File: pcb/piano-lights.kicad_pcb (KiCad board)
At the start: 2 copper layers, 98 x 51.6 mm, 41 parts, among them J1 USB-C 6-Pin, J2 FTDI RS232, J3 LED Strip, J4 AVR-ISP-6, J5 MIDI IN, J6 MIDI THRU, J7 MIDI Coupler B, J8 MIDI Coupler A, SW1 Button, SW2 Reset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

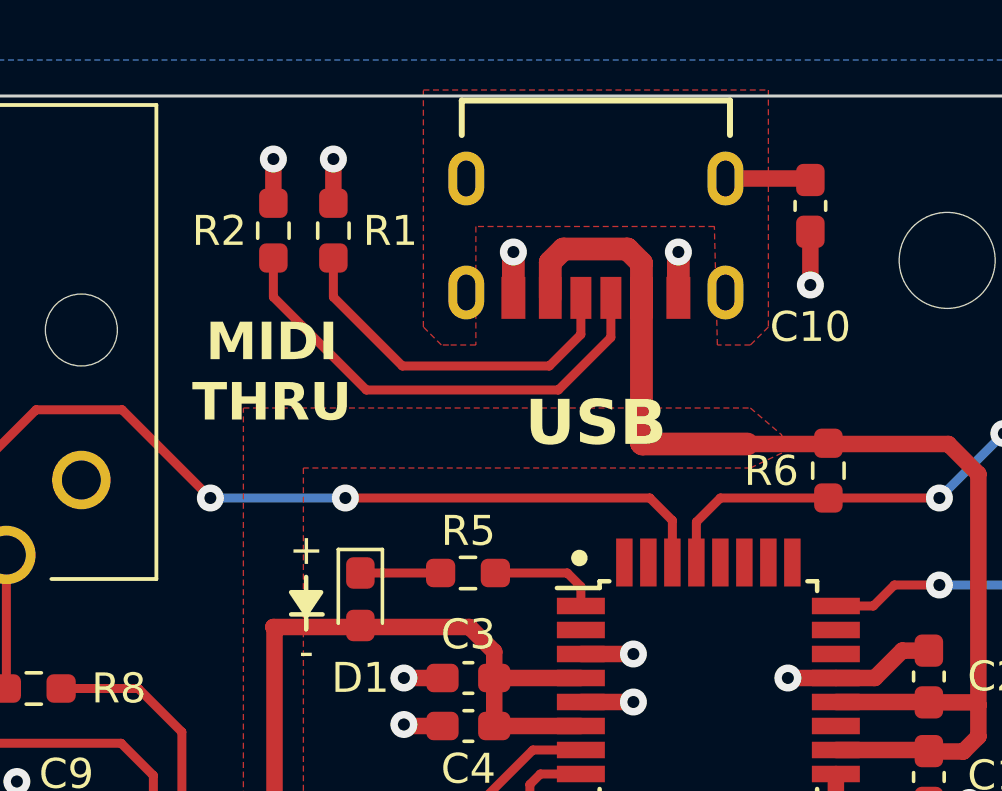
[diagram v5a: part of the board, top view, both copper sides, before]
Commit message: Move R1 and R2 again
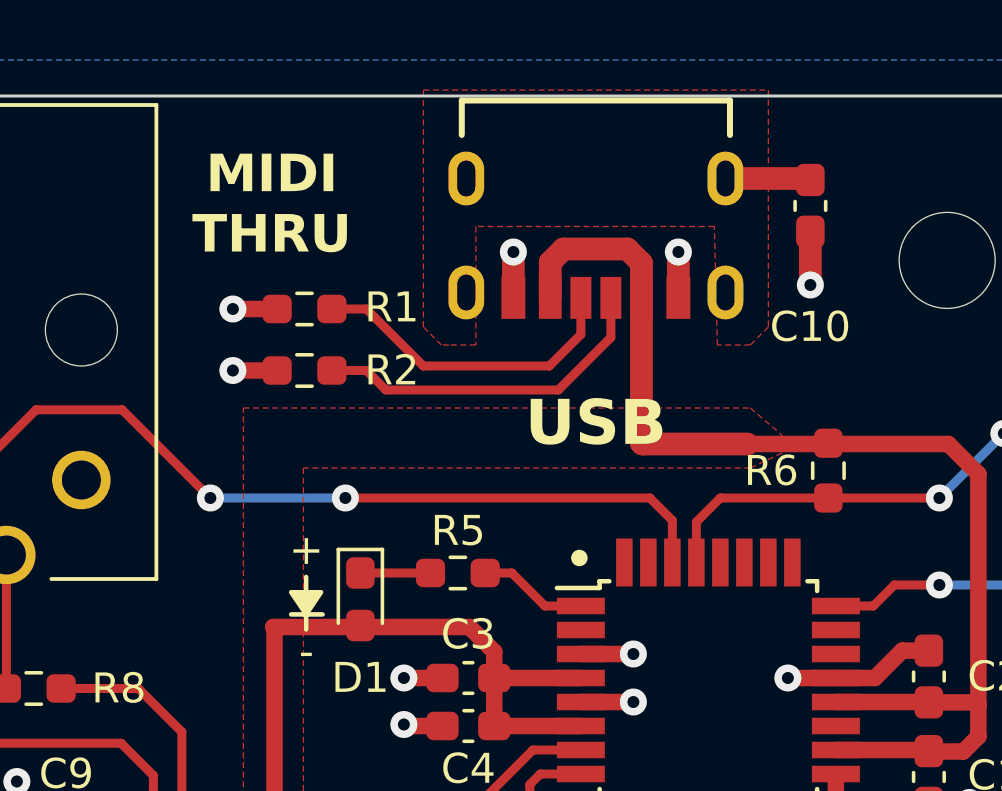
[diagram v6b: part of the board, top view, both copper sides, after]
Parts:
- moved R2 4.78 mm to (148.1, 87.3), turned to 180 degrees
- moved R1 2.78 mm to (148.1, 85.3), turned to 180 degrees
- moved R5 0.34 mm to (153.2, 94.1)
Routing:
- net /USB_CC1: track 15.9 -> 11.6 mm
- net /USB_CC2: track 12.2 -> 10.7 mm

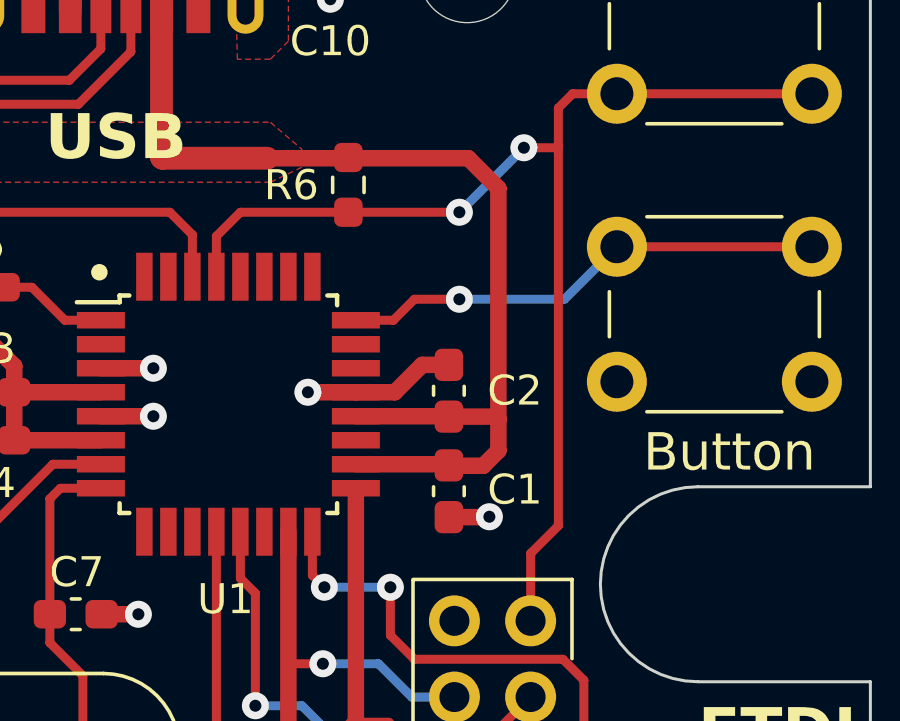
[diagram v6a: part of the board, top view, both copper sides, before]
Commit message: Rotate C1 and C2
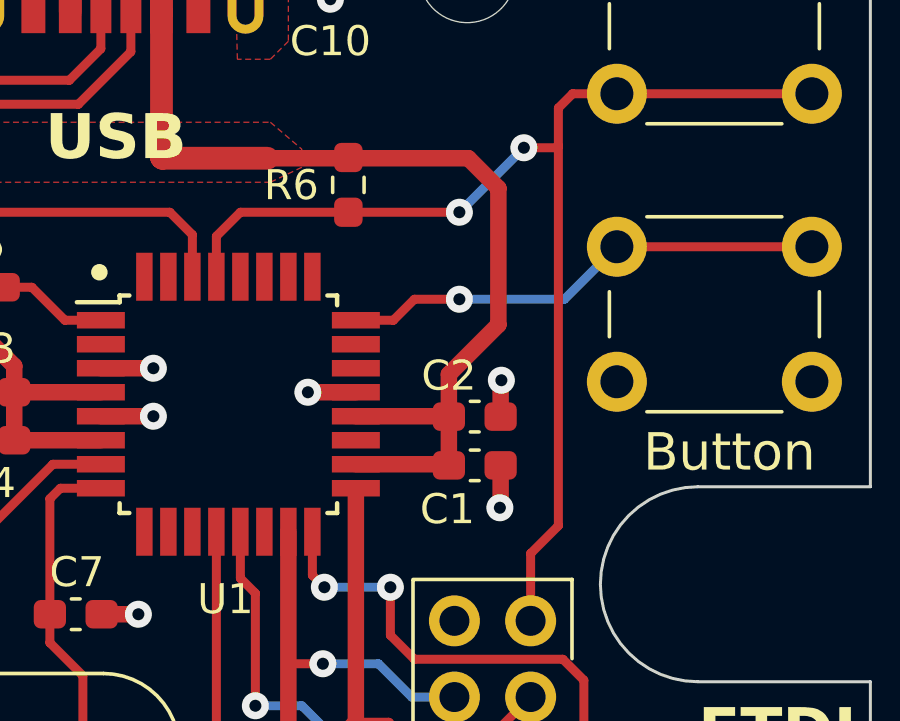
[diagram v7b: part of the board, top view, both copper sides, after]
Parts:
- moved C1 1.22 mm to (169.8, 100.0), turned to 0 degrees
- moved C2 1.22 mm to (169.8, 98.4), turned to 0 degrees
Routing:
- net +5V: track 133.0 -> 130.6 mm
- net GND: track 31.7 -> 29.5 mm, vias 18 -> 19

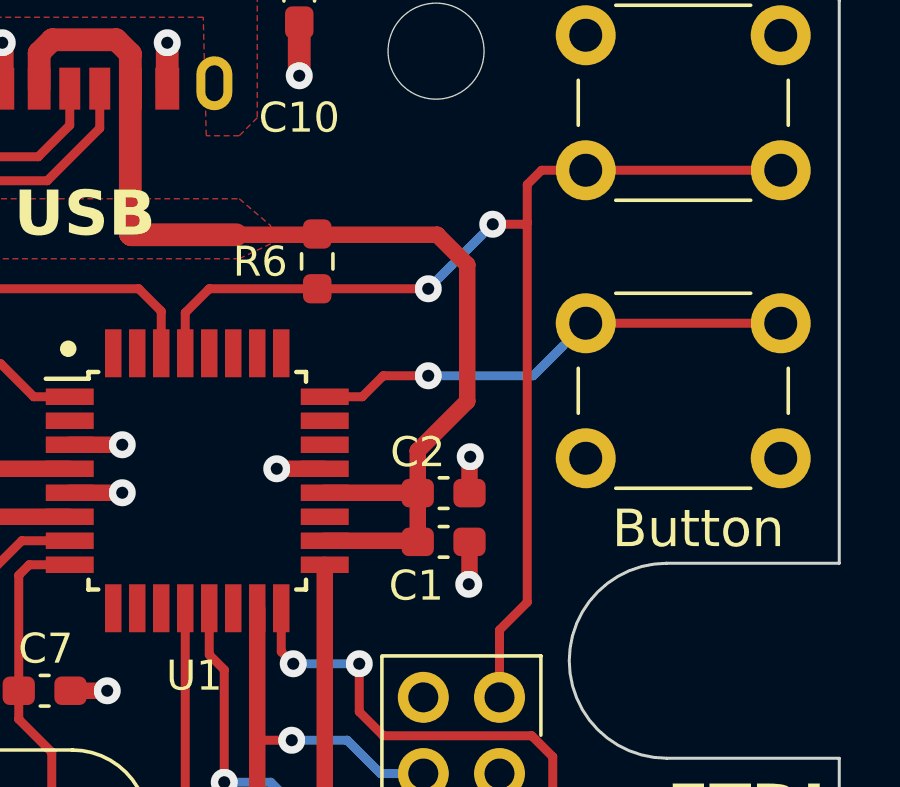
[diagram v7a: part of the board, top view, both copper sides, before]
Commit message: Reroute +5V to C1 and C2
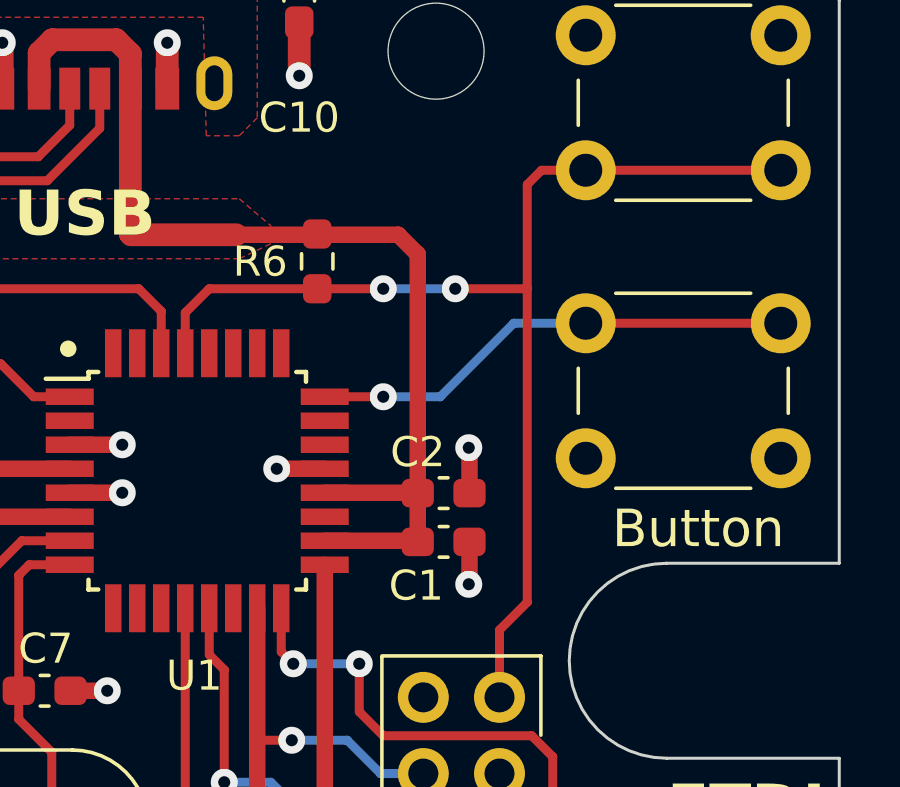
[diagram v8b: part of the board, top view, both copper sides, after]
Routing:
- net +5V: track 130.6 -> 128.5 mm
- net /~{RESET}: track 40.1 -> 39.2 mm
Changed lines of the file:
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@@
   (segment (start 157.35 100.8) (end 156 100.8) (width 0.3) (layer "F.Cu") (net 1))
   (segment (start 156.75 107.05) (end 156.75 109.5) (width 0.3) (layer "F.Cu") (net 1))
+  (segment (start 170.65 96.9) (end 170.675 96.925) (width 0.55) (layer "F.Cu") (net 2))
   (segment (start 132.46 102.24) (end 132.45 102.25) (width 0.55) (layer "F.Cu") (net 2))
   (segment (start 147.225 87.35) (end 145.75 87.35) (width 0.55) (layer "F.Cu") (net 2))
-  (segment (start 170.675 97.225) (end 170.7 97.2) (width 0.55) (layer "F.Cu") (net 2))
-  (segment (start 170.675 98.4125) (end 170.675 97.225) (width 0.55) (layer "F.Cu") (net 2))
+  (segment (start 170.675 96.925) (end 170.675 98.4125) (width 0.55) (layer "F.Cu") (net 2))
   (segment (start 155.1 84.93) (end 155.1 83.4) (width 0.76) (layer "F.Cu") (net 2))
   (segment (start 165.85 97.6) (end 164.25 97.6) (width 0.55) (layer "F.Cu") (net 2))
@@
   (via (at 160.6 83.4) (size 0.9) (drill 0.4) (layers "F.Cu" "B.Cu") (net 2))
   (via (at 159.1 98.4) (size 0.9) (drill 0.4) (layers "F.Cu" "B.Cu") (net 2))
-  (via (at 170.7 97.2) (size 0.9) (drill 0.4) (layers "F.Cu" "B.Cu") (net 2))
+  (via (at 170.65 96.9) (size 0.9) (drill 0.4) (layers "F.Cu" "B.Cu") (net 2))
   (via (at 158.6 105) (size 0.9) (drill 0.4) (layers "F.Cu" "B.Cu") (net 2))
   (via (at 132.45 102.25) (size 0.9) (drill 0.4) (layers "F.Cu" "B.Cu") (net 2))
@@
   (segment (start 155.75 100) (end 157.35 100) (width 0.3) (layer "F.Cu") (net 3))
   (segment (start 153 105) (end 153 102.75) (width 0.3) (layer "F.Cu") (net 3))
-  (segment (start 170.6 90.8) (end 169.6 89.8) (width 0.55) (layer "F.Cu") (net 4))
   (segment (start 159.37 83.77) (end 159.37 84.93) (width 0.76) (layer "F.Cu") (net 4))
   (segment (start 165.575 89.8) (end 165.6 89.775) (width 0.55) (layer "F.Cu") (net 4))
-  (segment (start 170.6 95.35) (end 170.6 90.8) (width 0.55) (layer "F.Cu") (net 4))
   (segment (start 154.05 121.65) (end 154.05 120.3) (width 0.55) (layer "F.Cu") (net 4))
   (segment (start 127 98.9) (end 126.375 98.275) (width 0.55) (layer "F.Cu") (net 4))
   (segment (start 168.9375 98.4) (end 168.95 98.4125) (width 0.55) (layer "F.Cu") (net 4))
   (segment (start 166.825 118.25) (end 162.475 122.6) (width 0.55) (layer "F.Cu") (net 4))
-  (segment (start 169.6 89.8) (end 165.625 89.8) (width 0.55) (layer "F.Cu") (net 4))
-  (segment (start 165.625 89.8) (end 165.6 89.775) (width 0.55) (layer "F.Cu") (net 4))
   (segment (start 155 122.6) (end 154.05 121.65) (width 0.55) (layer "F.Cu") (net 4))
   (segment (start 147.1375 110.2375) (end 147.1375 95.9375) (width 0.55) (layer "F.Cu") (net 4))
@@
   (segment (start 129.92 99.775) (end 127 99.775) (width 0.55) (layer "F.Cu") (net 4))
   (segment (start 153.6375 95.9) (end 154.4625 96.725) (width 0.55) (layer "F.Cu") (net 4))
-  (segment (start 168.95 97) (end 170.6 95.35) (width 0.55) (layer "F.Cu") (net 4))
   (segment (start 156.77 83.3) (end 158.9 83.3) (width 0.76) (layer "F.Cu") (net 4))
   (segment (start 140.25 102.45) (end 142.15 102.45) (width 0.55) (layer "F.Cu") (net 4))
@@
   (segment (start 165.85 100) (end 168.9125 100) (width 0.55) (layer "F.Cu") (net 4))
   (segment (start 169.1 118.25) (end 166.825 118.25) (width 0.55) (layer "F.Cu") (net 4))
+  (segment (start 165.625 89.8) (end 165.6 89.775) (width 0.55) (layer "F.Cu") (net 4))
   (segment (start 156.33 84.93) (end 156.33 83.74) (width 0.76) (layer "F.Cu") (net 4))
   (segment (start 131.825 104.35) (end 140.225 104.35) (width 0.55) (layer "F.Cu") (net 4))
   (segment (start 165.85 98.4) (end 168.9375 98.4) (width 0.55) (layer "F.Cu") (net 4))
-  (segment (start 168.95 98.4125) (end 168.95 97) (width 0.55) (layer "F.Cu") (net 4))
   (segment (start 126.375 98.275) (end 126.375 97.575) (width 0.55) (layer "F.Cu") (net 4))
   (segment (start 140.25 102.45) (end 140.25 108.925) (width 0.55) (layer "F.Cu") (net 4))
@@
   (segment (start 157.35 99.2) (end 154.4625 99.2) (width 0.55) (layer "F.Cu") (net 4))
   (segment (start 129.92 99.775) (end 129.92 102.445) (width 0.55) (layer "F.Cu") (net 4))
+  (segment (start 168.95 98.4125) (end 168.95 90.45) (width 0.55) (layer "F.Cu") (net 4))
+  (segment (start 168.3 89.8) (end 165.625 89.8) (width 0.55) (layer "F.Cu") (net 4))
+  (segment (start 168.95 90.45) (end 168.3 89.8) (width 0.55) (layer "F.Cu") (net 4))
   (segment (start 147.1 95.9) (end 153.6375 95.9) (width 0.55) (layer "F.Cu") (net 4))
   (segment (start 159.37 84.93) (end 159.37 89.77) (width 0.76) (layer "F.Cu") (net 4))
@@
   (via (at 167 104.1) (size 0.9) (drill 0.4) (layers "F.Cu" "B.Cu") (net 17))
   (segment (start 164.8 104.1) (end 167 104.1) (width 0.3) (layer "B.Cu") (net 17))
-  (segment (start 172.55 89.45) (end 172.6 89.4) (width 0.3) (layer "F.Cu") (net 18))
   (segment (start 171.675 105.22) (end 171.675 102.975) (width 0.3) (layer "F.Cu") (net 18))
   (segment (start 161.2 93.75) (end 161.2 92.4) (width 0.3) (layer "F.Cu") (net 18))
-  (segment (start 165.6 91.6) (end 169.3 91.6) (width 0.3) (layer "F.Cu") (net 18))
-  (segment (start 171.45 89.45) (end 172.55 89.45) (width 0.3) (layer "F.Cu") (net 18))
+  (segment (start 165.6 91.6) (end 167.8 91.6) (width 0.3) (layer "F.Cu") (net 18))
+  (segment (start 172.6 91.6) (end 172.6 88.125) (width 0.3) (layer "F.Cu") (net 18))
+  (segment (start 170.2 91.6) (end 172.6 91.6) (width 0.3) (layer "F.Cu") (net 18))
   (segment (start 173.075 87.65) (end 174.55 87.65) (width 0.3) (layer "F.Cu") (net 18))
   (segment (start 171.675 102.975) (end 172.6 102.05) (width 0.3) (layer "F.Cu") (net 18))
-  (segment (start 172.6 89.4) (end 172.6 88.125) (width 0.3) (layer "F.Cu") (net 18))
   (segment (start 161.2 92.4) (end 162 91.6) (width 0.3) (layer "F.Cu") (net 18))
   (segment (start 172.6 88.125) (end 173.075 87.65) (width 0.3) (layer "F.Cu") (net 18))
-  (segment (start 172.6 102.05) (end 172.6 89.4) (width 0.3) (layer "F.Cu") (net 18))
+  (segment (start 172.6 102.05) (end 172.6 91.6) (width 0.3) (layer "F.Cu") (net 18))
   (segment (start 162 91.6) (end 165.6 91.6) (width 0.3) (layer "F.Cu") (net 18))
   (segment (start 174.55 87.65) (end 181.05 87.65) (width 0.3) (layer "F.Cu") (net 18))
-  (via (at 169.3 91.6) (size 0.9) (drill 0.4) (layers "F.Cu" "B.Cu") (net 18))
-  (via (at 171.45 89.45) (size 0.9) (drill 0.4) (layers "F.Cu" "B.Cu") (net 18))
-  (segment (start 169.3 91.6) (end 171.45 89.45) (width 0.3) (layer "B.Cu") (net 18))
+  (via (at 170.2 91.6) (size 0.9) (drill 0.4) (layers "F.Cu" "B.Cu") (net 18))
+  (via (at 167.8 91.6) (size 0.9) (drill 0.4) (layers "F.Cu" "B.Cu") (net 18))
+  (segment (start 167.8 91.6) (end 170.2 91.6) (width 0.3) (layer "B.Cu") (net 18))
   (segment (start 165.15 111.8) (end 169.2 115.85) (width 0.3) (layer "F.Cu") (net 23))
   (segment (start 169.2 115.85) (end 178.73 115.85) (width 0.3) (layer "F.Cu") (net 23))
@@
   (segment (start 155.05 94.1) (end 154.1625 94.1) (width 0.3) (layer "F.Cu") (net 31))
   (segment (start 157.35 95.2) (end 156.15 95.2) (width 0.3) (layer "F.Cu") (net 31))
-  (segment (start 165.85 95.2) (end 167.1 95.2) (width 0.3) (layer "F.Cu") (net 39))
-  (segment (start 167.1 95.2) (end 167.8 94.5) (width 0.3) (layer "F.Cu") (net 39))
-  (segment (start 167.8 94.5) (end 169.3 94.5) (width 0.3) (layer "F.Cu") (net 39))
+  (segment (start 165.85 95.2) (end 167.8 95.2) (width 0.3) (layer "F.Cu") (net 39))
   (segment (start 174.55 92.75) (end 181.05 92.75) (width 0.3) (layer "F.Cu") (net 39))
-  (via (at 169.3 94.5) (size 0.9) (drill 0.4) (layers "F.Cu" "B.Cu") (net 39))
-  (segment (start 169.3 94.5) (end 172.8 94.5) (width 0.3) (layer "B.Cu") (net 39))
-  (segment (start 172.8 94.5) (end 174.55 92.75) (width 0.3) (layer "B.Cu") (net 39))
+  (via (at 167.8 95.2) (size 0.9) (drill 0.4) (layers "F.Cu" "B.Cu") (net 39))
+  (segment (start 169.7 95.2) (end 172.15 92.75) (width 0.3) (layer "B.Cu") (net 39))
+  (segment (start 172.15 92.75) (end 174.55 92.75) (width 0.3) (layer "B.Cu") (net 39))
+  (segment (start 167.8 95.2) (end 169.7 95.2) (width 0.3) (layer "B.Cu") (net 39))
   (segment (start 130.7 127) (end 135.7 127) (width 0.55) (layer "F.Cu") (net 44))
   (segment (start 107.5 93.5) (end 113 93.5) (width 0.55) (layer "F.Cu") (net 48))
